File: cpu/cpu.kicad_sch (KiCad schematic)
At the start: 40 parts, among them J2 Conn_01x08, Q3 2N7002, U1 ICE40HX1K-VQ100_RV4028, U2 W25Q80DVSS, U3 AP2112K-1.2

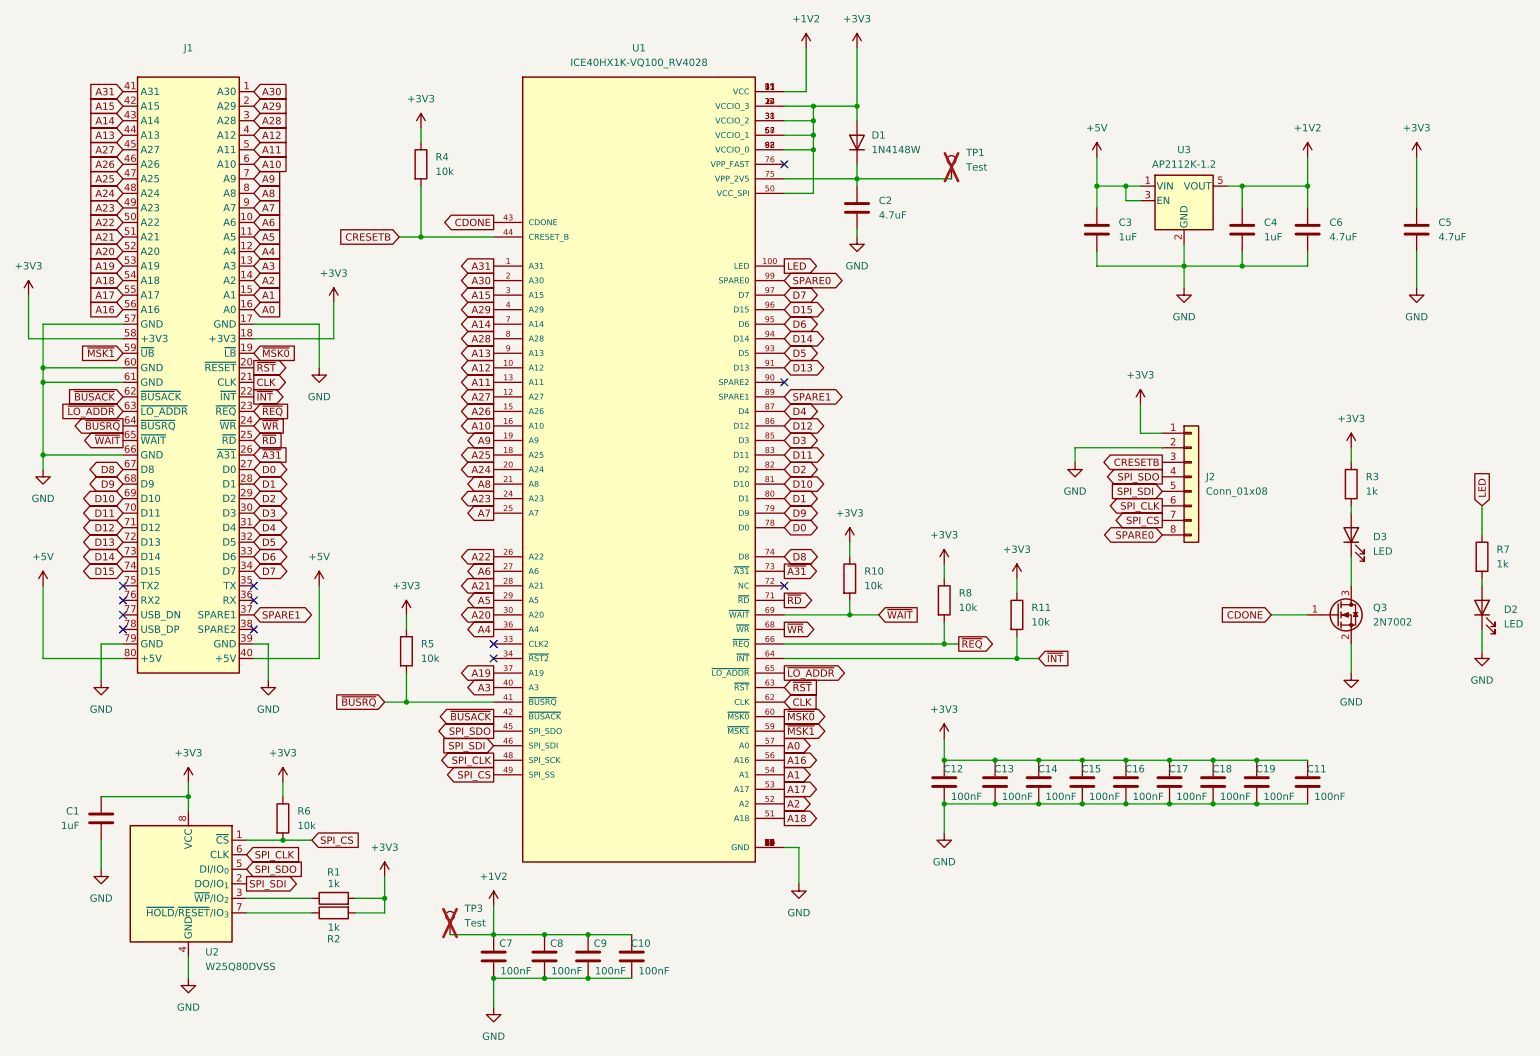
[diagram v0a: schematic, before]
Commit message: Updates from ICE40 checklist
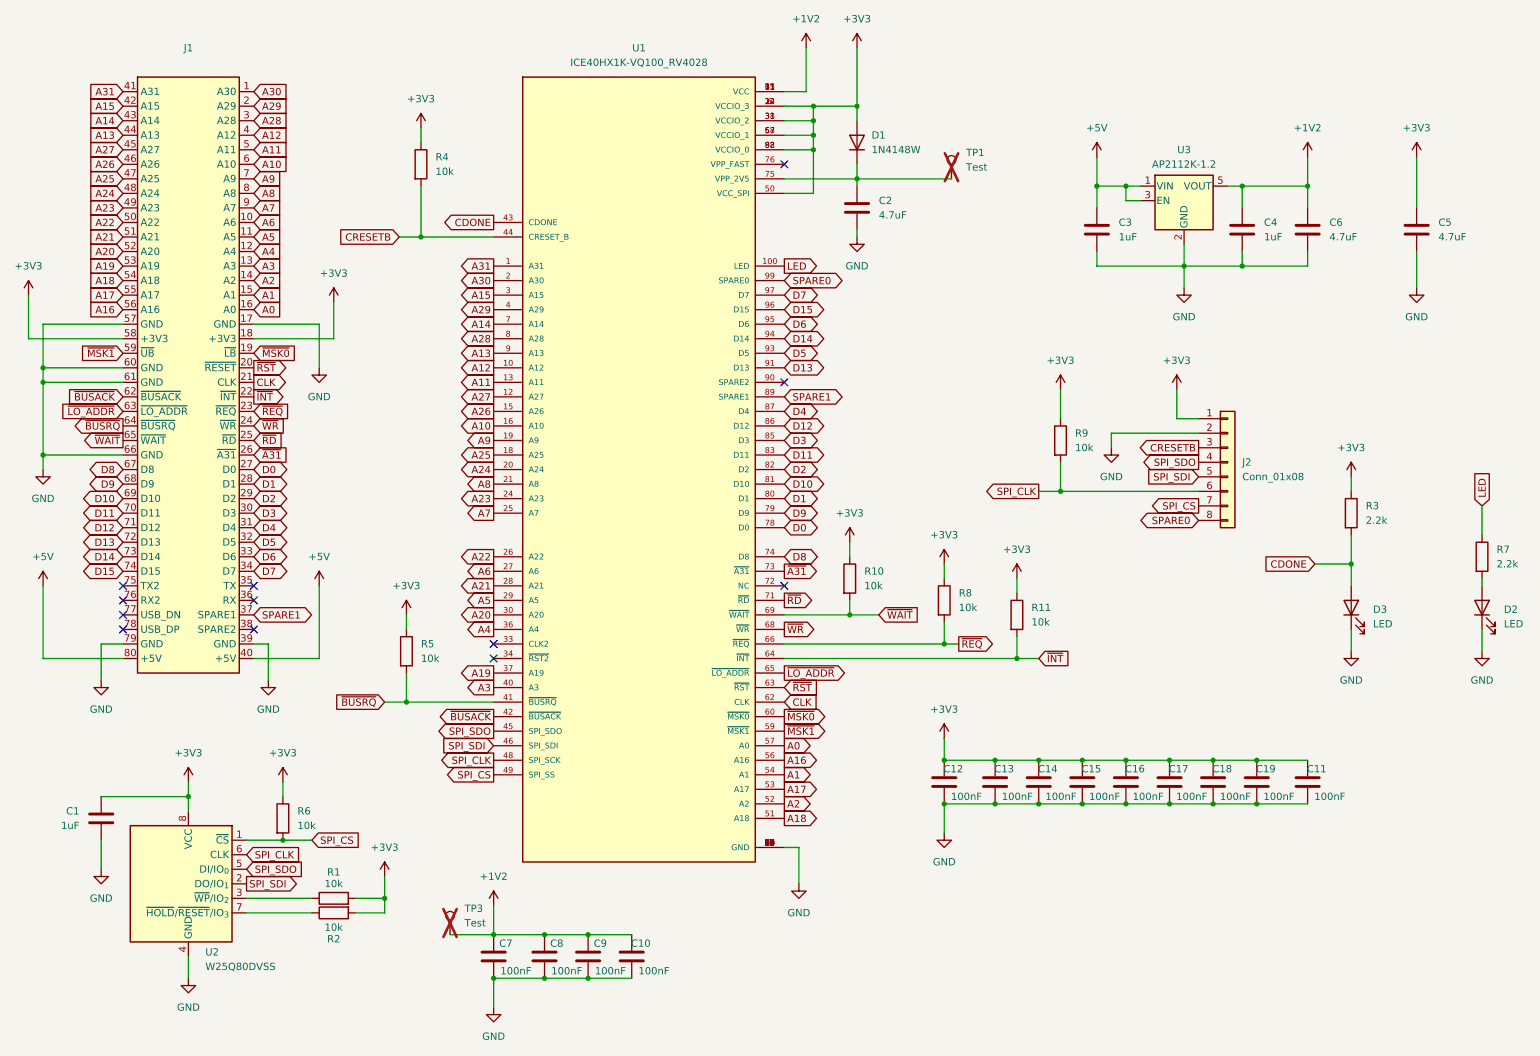
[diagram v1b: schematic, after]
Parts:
- removed Q3: 2N7002, Package_TO_SOT_SMD:SOT-23, symbol Transistor_FET:2N7002
- added R9: 10k, Resistor_SMD:R_0402_1005Metric, symbol Device:R
- R1, R2: value 1k -> 10k; JLC C11702 -> C25744
- R3, R7: value 1k -> 2.2k; JLC C11702 -> C25879
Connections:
- net +3V3: now also R9.1
- net CDONE: now also D3.2 (A), R3.2
- net GND: now also D3.1 (K)
- net SPI_CLK: now also R9.2
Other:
- moved on the sheet: D3, J2, R3
